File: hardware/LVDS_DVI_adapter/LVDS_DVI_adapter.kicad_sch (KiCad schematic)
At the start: 19 parts, among them J1 DF12NB(3.0)-30DS-0.5V(51), J2 HDMI_A, J3 LiteFury, U1 TXS0102DCU

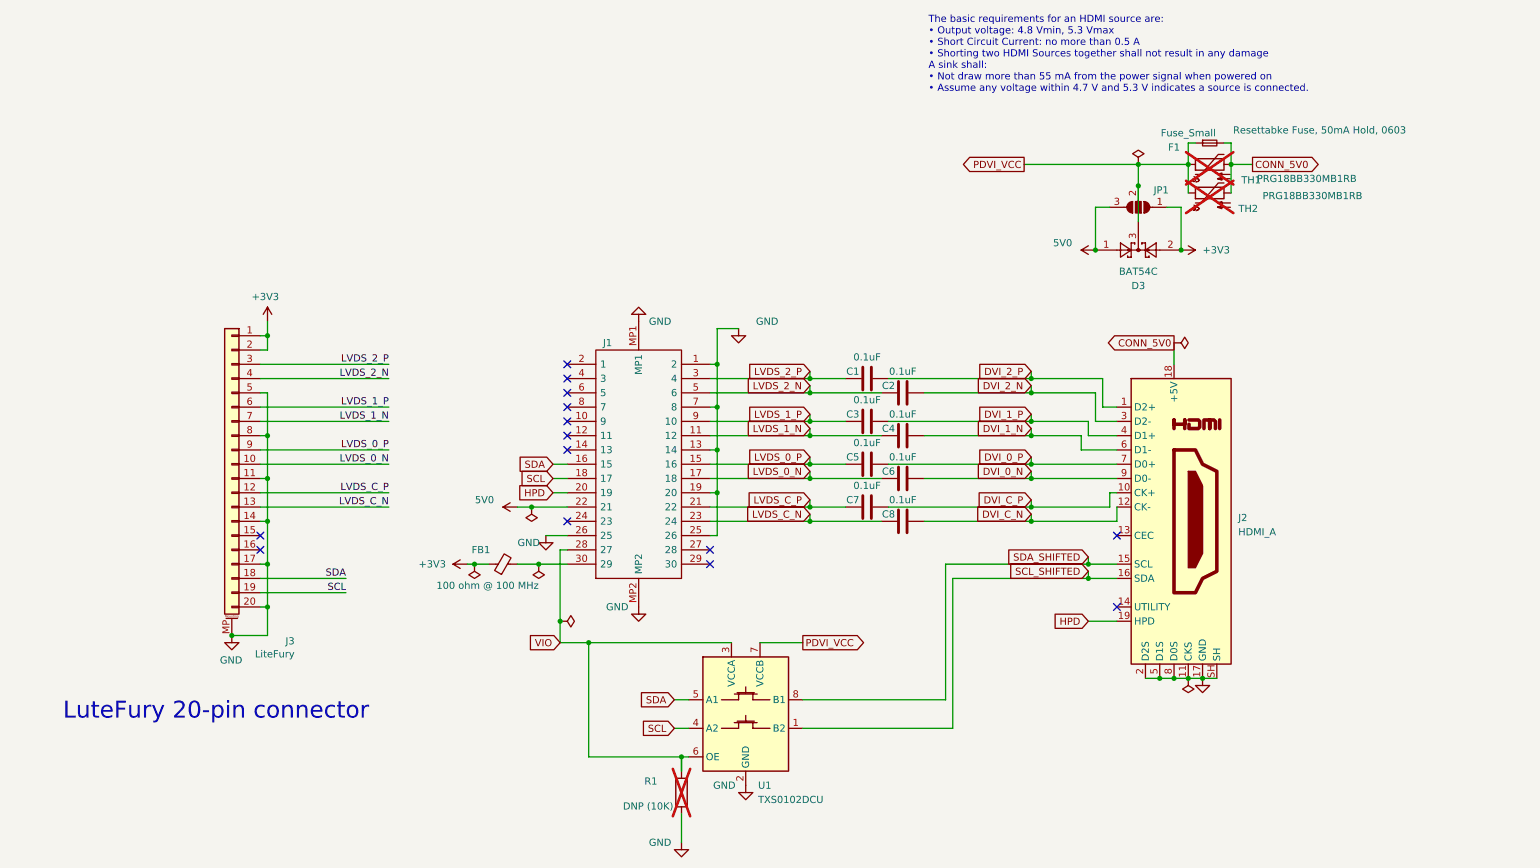
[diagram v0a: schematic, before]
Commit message: Add 3.3V to 5V pump as DVI power (HE9009M6R) and general fixes
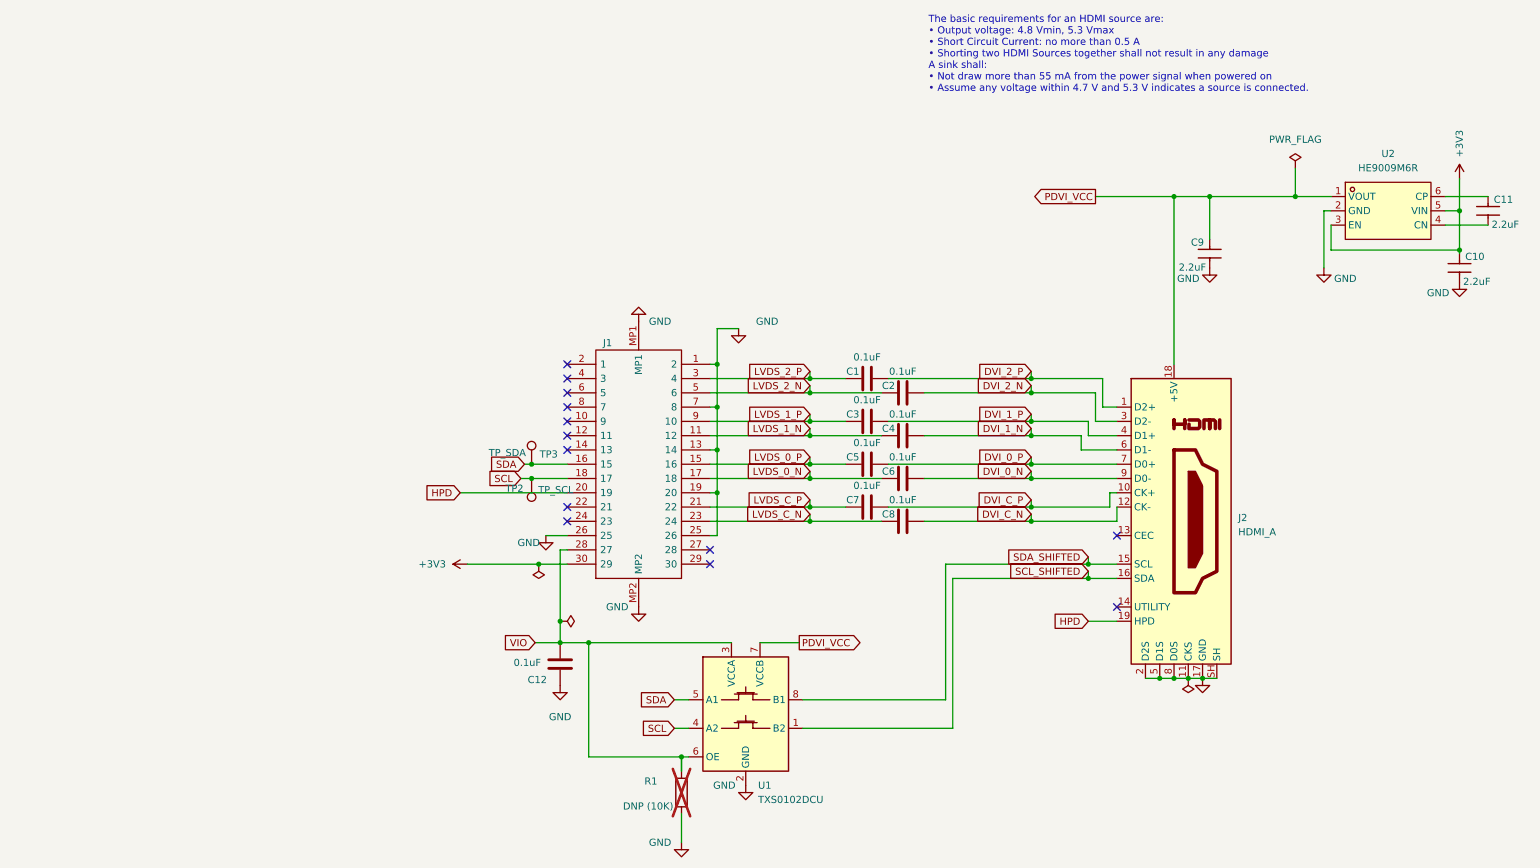
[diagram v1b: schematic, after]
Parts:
- removed D3: BAT54C, Package_TO_SOT_SMD:SOT-23, symbol Diode:BAT54C
- removed F1: Fuse_Small, Fuse:Fuse_0603_1608Metric, symbol Device:Fuse_Small
- removed FB1: 100 ohm @ 100 MHz, Inductor_SMD:L_0603_1608Metric, symbol Device:FerriteBead_Small
- removed J3: LiteFury, Library:Hirose_DF52-20S-0.8H_1x20-1MP_P0.80mm_Horizontal, symbol Connector_Generic_MountingPin:Conn_01x20_MountingPin
- removed JP1: SolderJumper_3_Open, Jumper:SolderJumper-3_P1.3mm_Open_RoundedPad1.0x1.5mm, symbol Jumper:SolderJumper_3_Open
- removed TH1, TH2: PRG18BB330MB1RB, Fuse:Fuse_0603_1608Metric, symbol Device:Thermistor_PTC
- added C10, C11, C9: 2.2uF, Capacitor_SMD:C_0402_1005Metric, symbol Periph-altium-import:0_CAP
- added C12: 0.1uF, Capacitor_SMD:C_0402_1005Metric, symbol Device:C
- added TP2: TP_SCL, TestPoint:TestPoint_THTPad_1.0x1.0mm_Drill0.5mm, symbol Connector:TestPoint
- added TP3: TP_SDA, TestPoint:TestPoint_THTPad_1.0x1.0mm_Drill0.5mm, symbol Connector:TestPoint
- added U2: HE9009M6R, Package_TO_SOT_SMD:SOT-23-6, symbol easyeda2kicad:HE9009M6R
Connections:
- net CONN_5V0 is gone; now on net PDVI_VCC: J2.18 (+5V)
- net +3V3: now also J1.30 (29), C10.1, U2.3 (EN), U2.5 (VIN)
- net GND: now also C10.2, C12.1, C9.2, U2.2 (GND)
- net PDVI_VCC: now also C9.1, U2.1 (VOUT)
- net SCL: now also TP2.1
- net SDA: now also TP3.1
- net VIO: now also C12.2
- net 5V0: no longer names the net of J1.22 (21)
- new net: C11.2, U2.4 (CN)
- new net: C11.1, U2.6 (CP)
- no-connect marks 14 -> 13
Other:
- note removed: "LuteFury 20-pin connector"
